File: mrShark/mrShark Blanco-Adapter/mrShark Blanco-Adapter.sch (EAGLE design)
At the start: 1 part, among them CON1 DF12-20DS

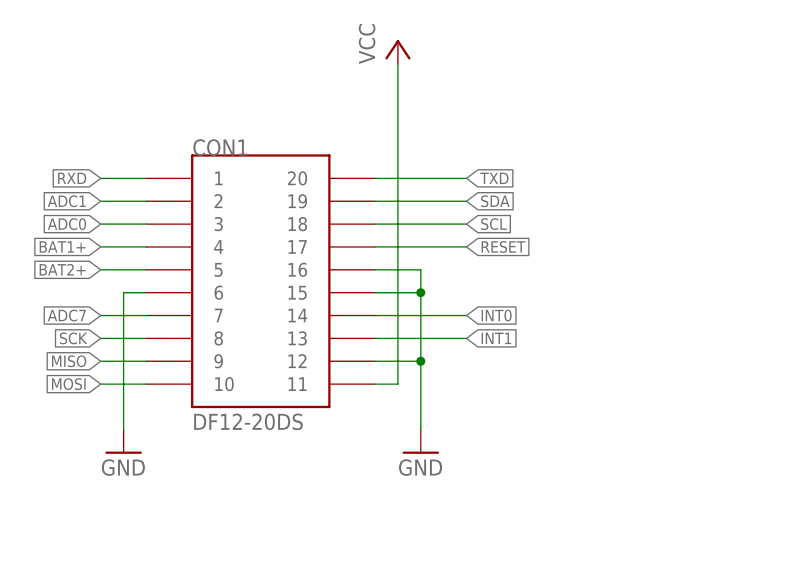
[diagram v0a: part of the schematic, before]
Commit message: Updated mrShark 1.2 & 1.3 Updated mrShark Adapter Updated mrShark LED-Marker to version 0.0.3
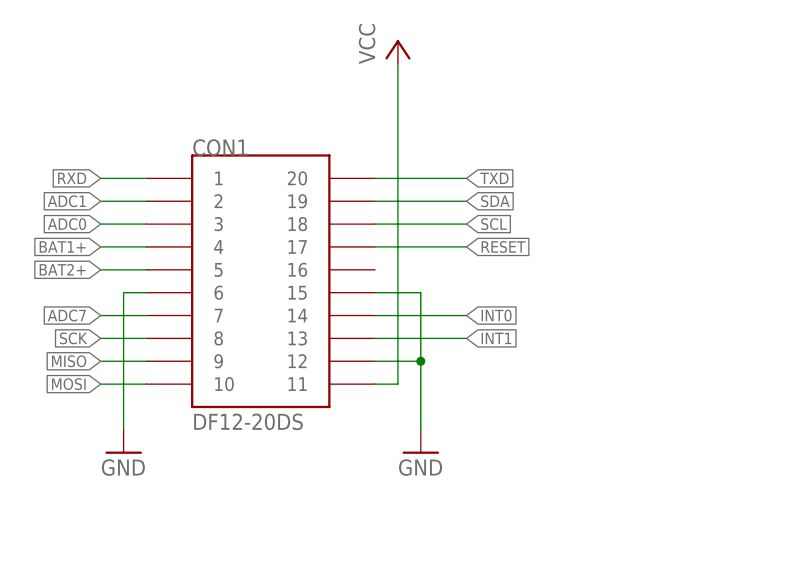
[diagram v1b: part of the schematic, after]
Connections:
- net GND: no longer CON1.16
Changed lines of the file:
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@@
 <?xml version="1.0" encoding="utf-8"?>
 <!DOCTYPE eagle SYSTEM "eagle.dtd">
-<eagle version="6.1">
+<eagle version="6.3">
 <drawing>
 <settings>
@@
 <pinref part="CON1" gate="CON$1" pin="15"/>
 <wire x1="124.46" y1="127" x2="129.54" y2="127" width="0.1524" layer="91"/>
-<wire x1="129.54" y1="127" x2="129.54" y2="129.54" width="0.1524" layer="91"/>
-<pinref part="CON1" gate="CON$1" pin="16"/>
-<wire x1="129.54" y1="129.54" x2="124.46" y2="129.54" width="0.1524" layer="91"/>
 <pinref part="CON1" gate="CON$1" pin="12"/>
 <wire x1="124.46" y1="119.38" x2="129.54" y2="119.38" width="0.1524" layer="91"/>
 <wire x1="129.54" y1="119.38" x2="129.54" y2="127" width="0.1524" layer="91"/>
-<junction x="129.54" y="127"/>
 <pinref part="GND3" gate="1" pin="GND"/>
 <wire x1="129.54" y1="119.38" x2="129.54" y2="111.76" width="0.1524" layer="91"/>
